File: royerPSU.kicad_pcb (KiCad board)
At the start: 2 copper layers, 32 parts, among them J1 24VAC, J101 bass guitar input, J103 iso output, J104 XLR out, J2 XLR5, J3 iso output, J4 mic out, SW1 SW_SPDT

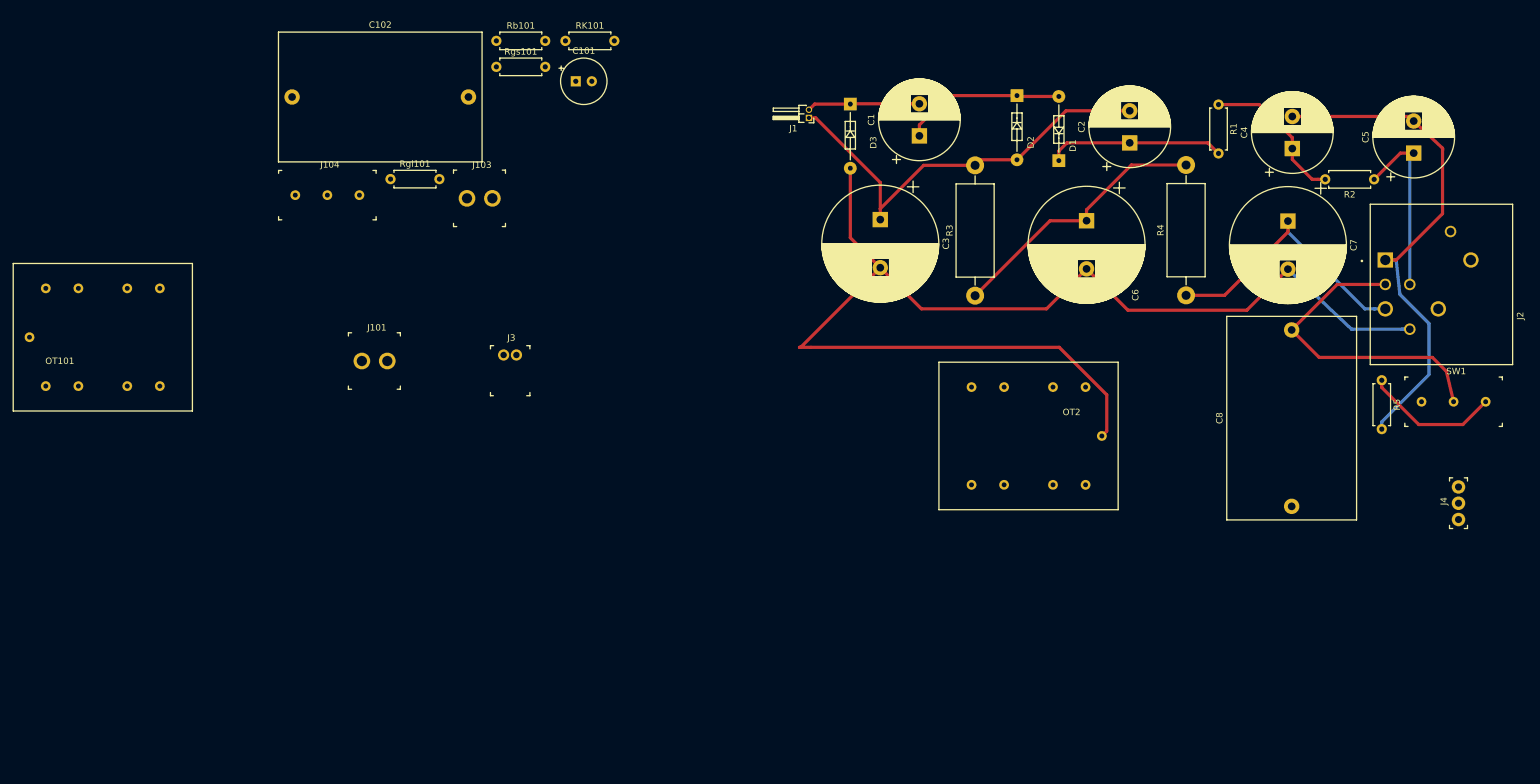
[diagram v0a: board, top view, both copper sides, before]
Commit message: mostly working layout of mic psu with cheapo output transformer still need chassis mounting and to choose 2 ground planes, and a way to link all the grunds toether at chassis complete this board as if the guitar portion is going to be a separate board will probably officially branch, or could rename this subproject and put it in a folder in git
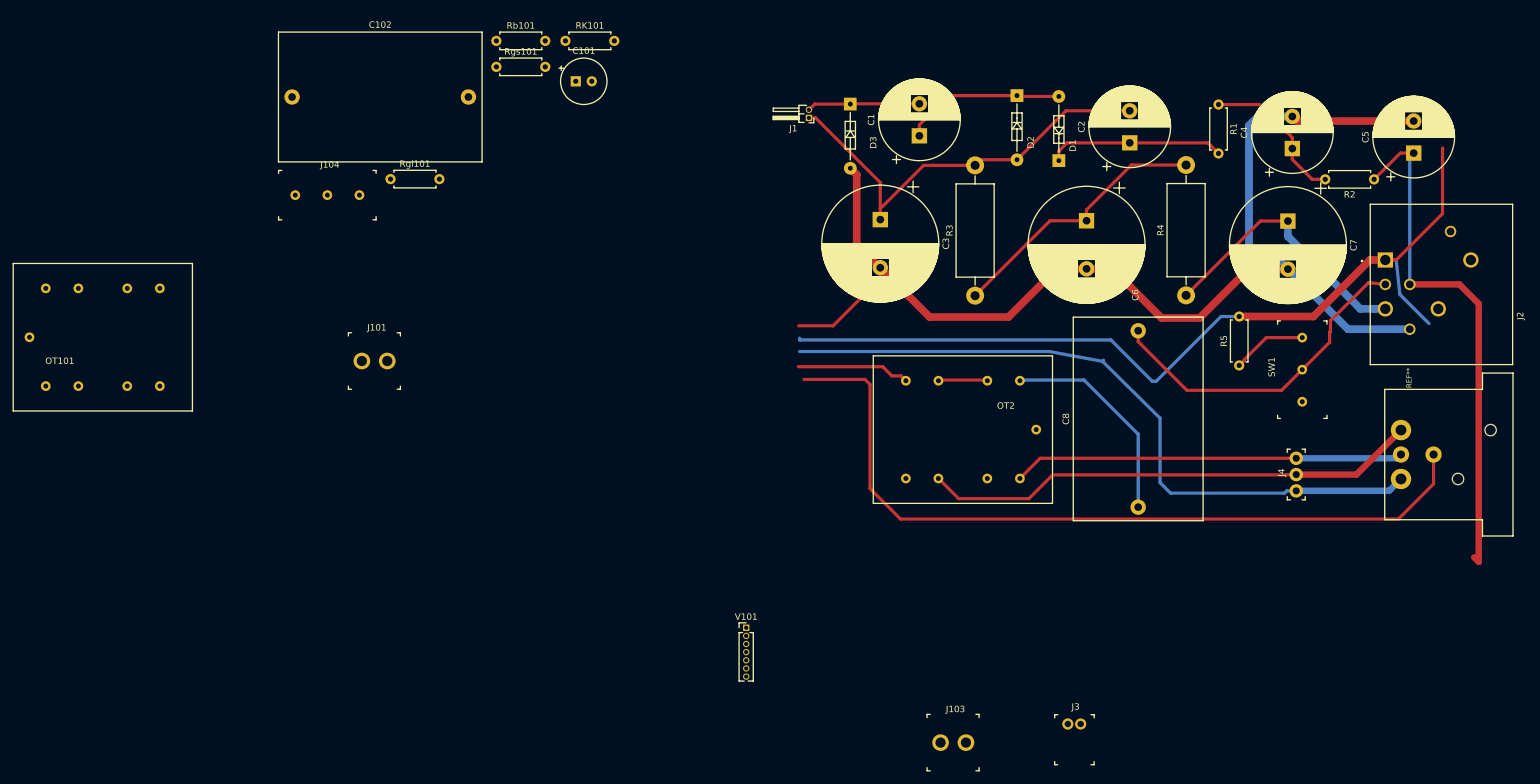
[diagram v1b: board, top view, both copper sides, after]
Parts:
- added REF**: NC3MBH, royerPSU:NC3MBH, F.Cu at (172.5, 119.5)
- added V101: S290MS001P003, Connector_PinHeader_1.27mm:PinHeader_1x07_P1.27mm_Vertical, F.Cu at (65.4, 146.5)
- moved J103 112.5 mm to (95.7, 164.4)
- moved J3 105.1 mm to (115.5, 161.5)
- moved J4 25.7 mm to (151.1, 125.2)
- moved C8 23.9 mm to (126.5, 127.7)
- moved R5 22.3 mm to (142.2, 105.6), turned to 90 degrees
- moved SW1 18.6 mm to (152.0, 111.3), turned to 90 degrees
- moved OT2 10.3 mm to (113.2, 127.1)
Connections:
- C3 pad 2: Earth -> -BATT
- C4 pad 2: Earth -> -BATT
- C5 pad 2: Earth -> -BATT
- C6 pad 2: Earth -> -BATT
- C7 pad 2: Earth -> -BATT
- D3 pad 2: Earth -> -BATT
- J2 pad 4: Earth -> -BATT
- J2 pad 6: (no net) -> Net-(J2-Pad6)
- J2 pad 7: (no net) -> Net-(J2-Pad6)
- J2 pad 8: (no net) -> Net-(J2-Pad6)
- OT2 pad P1+: Net-(J4-Pad2) -> Net-(J4-Pad3)
- OT2 pad P1-: Net-(J4-Pad3) -> Net-(J4-Pad2)
- OT2 pad Screen: Earth -> GNDPWR
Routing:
- net -BATT: track 0.00 -> 187.9 mm
- net Earth: track 271.8 -> 389.2 mm
- net Net-(J4-Pad2): track 0.00 -> 77.8 mm
- net Net-(J4-Pad3): track 0.00 -> 61.2 mm
- net HT: track 28.6 -> 81.8 mm
- net Net-(C8-Pad1): track 0.00 -> 33.5 mm
- net Net-(R5-Pad1): track 21.2 -> 11.7 mm
- net Net-(OT2-PadS1-): track 0.00 -> 7.62 mm
- net micSig: track 49.2 -> 52.2 mm
- net +6V: track 43.6 -> 43.1 mm

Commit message: defined mounting holes, and 1 chassis mounting hole and star ground point removed all guitar related parts to create the royermod psu on its own need to define switch to toggle 39k cathode resistor
exported gerbers for test build

still need:
front panel
bom
will define this as a release after double checking
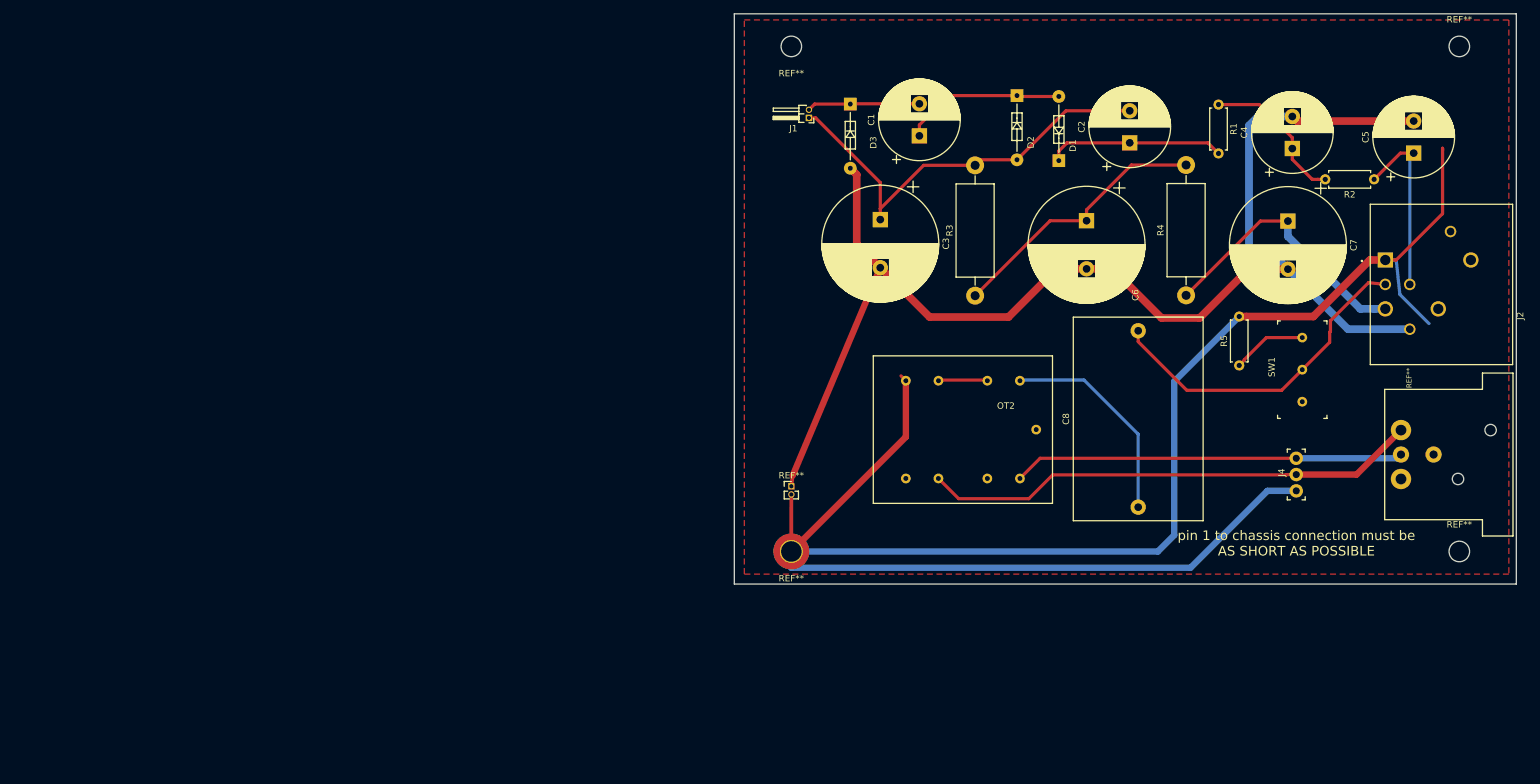
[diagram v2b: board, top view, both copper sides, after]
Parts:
- removed C101: 22n, Capacitor_THT:CP_Radial_Tantal_D7.0mm_P2.50mm
- removed C102: 2u2, Capacitor_THT:C_Rect_L31.5mm_W20.0mm_P27.50mm_MKS4
- removed J101: bass guitar input, digikey:PinHeader_1x2_P3.96mm_Drill1.6mm
- removed J103: iso output, digikey:PinHeader_1x2_P3.96mm_Drill1.6mm
- removed J104: XLR out, digikey:Term_Block_1x3_P5mm
- removed J3: iso output, digikey:PinHeader_1x2_P2mm_Drill1mm_RA
- removed OT101: A262A2E, royerPSU:ae262a3E
- removed RK101: 5k, Resistor_THT:R_Axial_DIN0207_L6.3mm_D2.5mm_P7.62mm_Horizontal
- removed Rb101: 160, Resistor_THT:R_Axial_DIN0207_L6.3mm_D2.5mm_P7.62mm_Horizontal
- removed Rgl101: 4M4, Resistor_THT:R_Axial_DIN0207_L6.3mm_D2.5mm_P7.62mm_Horizontal
- removed Rgs101: 1k, Resistor_THT:R_Axial_DIN0207_L6.3mm_D2.5mm_P7.62mm_Horizontal
- removed V101: S290MS001P003, Connector_PinHeader_1.27mm:PinHeader_1x07_P1.27mm_Vertical
- added REF**: PinHeader_1x02_P1.27mm_Vertical, Connector_PinHeader_1.27mm:PinHeader_1x02_P1.27mm_Vertical, F.Cu at (72.4, 124.5)
- added REF**: MountingHole_3.2mm_M3_DIN965_Pad_TopBottom, MountingHole:MountingHole_3.2mm_M3_DIN965_Pad_TopBottom, F.Cu at (72.4, 134.6)
- added REF**: MountingHole_3.2mm_M3, MountingHole:MountingHole_3.2mm_M3, F.Cu at (72.4, 55.9)
- added REF**: MountingHole_3.2mm_M3, MountingHole:MountingHole_3.2mm_M3, F.Cu at (176.5, 55.9)
- added REF**: MountingHole_3.2mm_M3, MountingHole:MountingHole_3.2mm_M3, F.Cu at (176.5, 134.6)
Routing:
- net Earth: track 389.2 -> 292.8 mm
- net HT: track 81.8 -> 28.6 mm
- net -BATT: track 187.9 -> 207.3 mm
- added copper zone on F.Cu, net Earth
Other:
- board outline added: 121.9 x 88.9 mm
- net class GND added: clearance 0.4, trace_width 0.5, via_dia 1, via_drill 0.5
- board text added: "pin 1 to chassis connection must be AS SHORT AS POSSIBLE"

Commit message: added some silk screen notes and makes small trace changes
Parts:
- J1: footprint Connector_PinHeader_1.27mm:PinHeader_1x02_P1.27mm_Horizontal -> Connector_Wire:SolderWire-0.75sqmm_1x02_P4.8mm_D1.25mm_OD2.3mm
- J2: value XLR5 -> NC5FAH
- jump this!: renamed from REF**
- xlr out: renamed from REF**
- moved J1 3.75 mm to (72.5, 69.7), turned to 90 degrees
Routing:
- net Earth: track 292.8 -> 257.6 mm
- net Net-(C1-Pad2): track 17.6 -> 25.5 mm
- net Net-(C2-Pad2): track 66.3 -> 70.1 mm
- net Net-(C1-Pad1): track 25.4 -> 23.6 mm
- net Net-(C2-Pad1): track 27.6 -> 26.4 mm

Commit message: exported current gerbers
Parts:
- removed REF**: MountingHole_3.2mm_M3_DIN965_Pad_TopBottom, MountingHole:MountingHole_3.2mm_M3_DIN965_Pad_TopBottom
- removed REF** (x2): MountingHole_3.2mm_M3, MountingHole:MountingHole_3.2mm_M3
- added  : MountingHole_3.2mm_M3, MountingHole:MountingHole_3.2mm_M3, F.Cu at (72.4, 55.9)
- added  : MountingHole_3.2mm_M3, MountingHole:MountingHole_3.2mm_M3, F.Cu at (176.5, 55.9)
- added EARTH: MountingHole_3.2mm_M3_DIN965_Pad_TopBottom, MountingHole:MountingHole_3.2mm_M3_DIN965_Pad_TopBottom, F.Cu at (72.4, 134.6)
-  : renamed from REF**
- cathode resistor: renamed from SW1; value SW_SPDT -> SPDT toggle
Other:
- board text added: "1 GND 2 Plate 100V 3 audio out 4 Heater 0V 5 Heater 6V"
- board text added: "Layout by Chris Williams 2021 Revision: 1"
- board text added: "Royer 2 PSU with adapted pinout and cathode resistor bypass"
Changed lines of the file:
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@@
   (general
     (thickness 1.6)
-    (drawings 2)
+    (drawings 5)
     (tracks 125)
     (zones 0)
@@
     (mod_text_size 1 1)
     (mod_text_width 0.15)
-    (pad_size 3.2 3.2)
-    (pad_drill 3.2)
+    (pad_size 2.4 2.4)
+    (pad_drill 1.6)
     (pad_to_mask_clearance 0.051)
     (solder_mask_min_width 0.25)
@@
     (tags "mounting hole 3.2mm m3 din965")
     (attr virtual)
-    (fp_text reference REF** (at 0 -4.2) (layer F.SilkS)
+    (fp_text reference EARTH (at 0 -4.2) (layer F.SilkS)
       (effects (font (size 1 1) (thickness 0.15)))
     )
@@
     (tags "mounting hole 3.2mm no annular m3")
     (attr virtual)
-    (fp_text reference REF** (at 0 -4.2) (layer F.SilkS)
+    (fp_text reference " " (at 0 -4.2) (layer F.SilkS)
       (effects (font (size 1 1) (thickness 0.15)))
     )
@@
     (tags "mounting hole 3.2mm no annular m3")
     (attr virtual)
-    (fp_text reference REF** (at 0 -4.2) (layer F.SilkS)
+    (fp_text reference " " (at 0 -4.2) (layer F.SilkS)
       (effects (font (size 1 1) (thickness 0.15)))
     )
@@
     (tags "mounting hole 3.2mm no annular m3")
     (attr virtual)
-    (fp_text reference REF** (at 0 -4.2) (layer F.SilkS)
+    (fp_text reference " " (at 0 -4.2) (layer F.SilkS)
       (effects (font (size 1 1) (thickness 0.15)))
     )
@@
     (at 152.0444 111.2774 90)
     (descr http://www.on-shore.com/wp-content/uploads/2015/09/osttcxx0162.pdf)
-    (fp_text reference SW1 (at 5.4 -4.75 90) (layer F.SilkS)
-      (effects (font (size 1 1) (thickness 0.15)))
-    )
-    (fp_text value SW_SPDT (at 5.4 4.85 90) (layer F.SilkS)
+    (fp_text reference "cathode resistor" (at 4.9784 -5.0038 90) (layer F.SilkS)
+      (effects (font (size 1 1) (thickness 0.15)))
+    )
+    (fp_text value "SPDT toggle" (at 4.4704 5.0292 90) (layer F.SilkS)
       (effects (font (size 1 1) (thickness 0.15)))
     )
@@
       (net 15 "Net-(SW1-Pad1)"))
   )
+  (gr_text "1 GND\n2 Plate 100V\n3 audio out\n4 Heater 0V\n5 Heater 6V" (at 81.9912 87.9856) (layer B.SilkS)
+    (effects (font (size 1.5 1.5) (thickness 0.3)) (justify left mirror))
+  )
+  (gr_text "Layout by Chris Williams\n2021  Revision: 1" (at 107.5182 115.7224) (layer B.Cu)
+    (effects (font (size 2.2 2.2) (thickness 0.35)) (justify left mirror))
+  )
+  (gr_text "Royer 2 PSU with adapted pinout and cathode resistor bypass" (at 124.3076 58.3692) (layer F.SilkS)
+    (effects (font (size 2 2) (thickness 0.5)))
+  )
   (gr_text "pin 1 to chassis connection must be\nAS SHORT AS POSSIBLE" (at 151.13 133.35) (layer F.SilkS)
